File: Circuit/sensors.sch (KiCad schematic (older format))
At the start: 6 parts, among them U301 BME280, U302 ADXL345

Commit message: More BOM - passives mostly.
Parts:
- R301, R302: Digikey PN (none) -> 311-4.7KGRCT-ND; Link (none) -> http://www.digikey.com.au/product-detail/en/yageo/RC0603JR-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; Manufacturer PN (none) -> RC0603JR-074K7L; Unit Cost (none) -> 0.10
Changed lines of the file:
@@
 Connection ~ 2500 2700
-$Comp
-L R R302
-U 1 1 564CDB75
-P 2250 3050
-F 0 "R302" V 2330 3050 50  0000 C CNN
-F 1 "4.7K" V 2250 3050 50  0000 C CNN
-F 2 "Resistors_SMD:R_0603_HandSoldering" V 2350 2850 24  0000 C CNN
-F 3 "" H 2250 3050 60  0000 C CNN
-	1    2250 3050
-	1    0    0    -1
-$EndComp
 $Comp
 L R R301
@@
 F 2 "Resistors_SMD:R_0603_HandSoldering" V 2150 2750 24  0000 C CNN
 F 3 "" H 2050 2950 60  0000 C CNN
+F 4 "311-4.7KGRCT-ND" V 2050 2950 60  0001 C CNN "Digikey PN"
+F 5 "http://www.digikey.com.au/product-detail/en/yageo/RC0603JR-074K7L/311-4.7KGRCT-ND/729732" V 2050 2950 60  0001 C CNN "Link"
+F 6 "RC0603JR-074K7L" V 2050 2950 60  0001 C CNN "Manufacturer PN"
+F 7 "0.10" V 2050 2950 60  0001 C CNN "Unit Cost"
 	1    2050 2950
 	1    0    0    -1
@@
 Text Notes 1200 1350 0    60   ~ 0
 Recommend different or removal. -BP
+$Comp
+L R R302
+U 1 1 58223067
+P 2250 3050
+F 0 "R302" V 2330 3050 50  0000 C CNN
+F 1 "4.7K" V 2250 3050 50  0000 C CNN
+F 2 "Resistors_SMD:R_0603_HandSoldering" V 2350 2850 24  0000 C CNN
+F 3 "" H 2250 3050 60  0000 C CNN
+F 4 "311-4.7KGRCT-ND" V 2250 3050 60  0001 C CNN "Digikey PN"
+F 5 "http://www.digikey.com.au/product-detail/en/yageo/RC0603JR-074K7L/311-4.7KGRCT-ND/729732" V 2250 3050 60  0001 C CNN "Link"
+F 6 "RC0603JR-074K7L" V 2250 3050 60  0001 C CNN "Manufacturer PN"
+F 7 "0.10" V 2250 3050 60  0001 C CNN "Unit Cost"
+	1    2250 3050
+	1    0    0    -1
+$EndComp
 $EndSCHEMATC

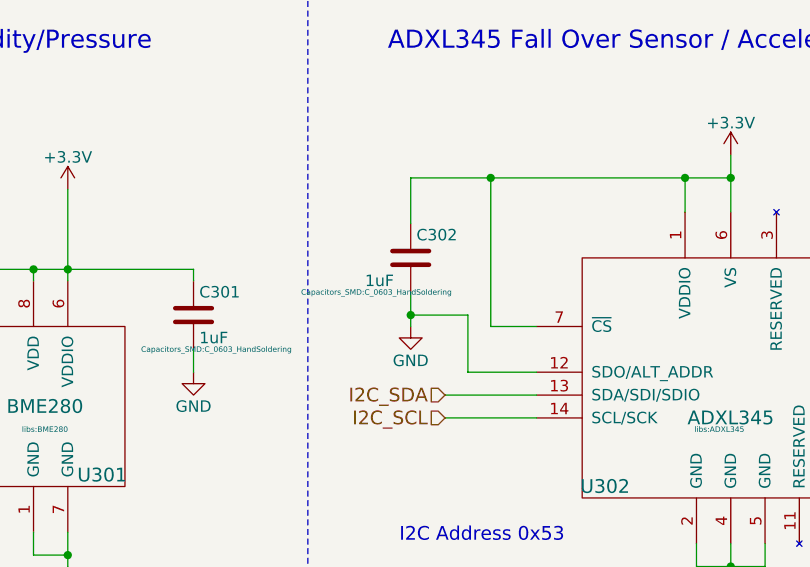
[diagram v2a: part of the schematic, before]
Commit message: Sensor ICs BOM information.
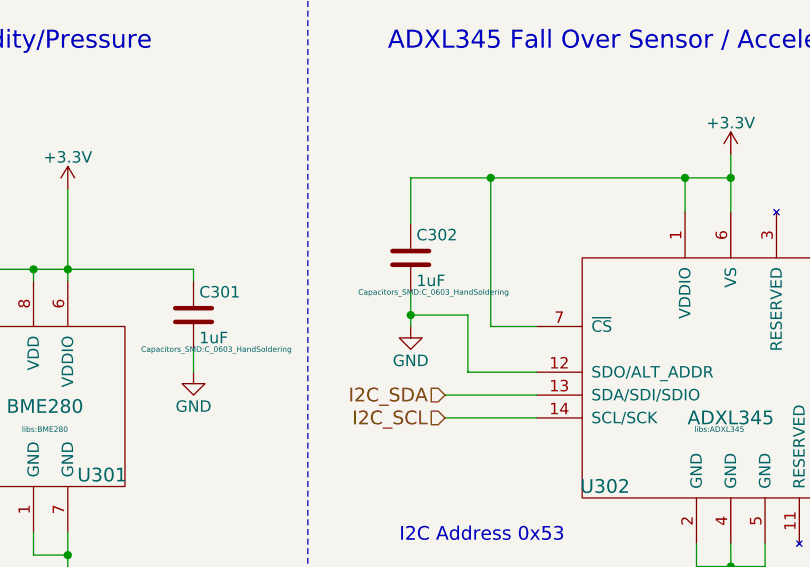
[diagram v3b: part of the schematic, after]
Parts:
- C301, C302: Digikey PN (none) -> 311-1372-1-ND; Link (none) -> http://www.digikey.com.au/product-detail/en/yageo/CC0603ZRY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; Manufacturer PN (none) -> CC0603ZRY5V7BB105; Unit Cost (none) -> 0.10
- U301: Digikey PN (none) -> 828-1063-1-ND; Link (none) -> http://www.digikey.com.au/product-detail/en/bosch-sensortec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; Manufacturer PN (none) -> BME280; Unit Cost (none) -> 11.00
- U302: Digikey PN (none) -> ADXL345BCCZ-RLCT-ND; Link (none) -> http://www.digikey.com.au/product-detail/en/analog-devices-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; Manufacturer PN (none) -> ADXL345BCCZ-RL; Unit Cost (none) -> 7.36
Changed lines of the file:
@@
 F 2 "libs:BME280" H 3150 3200 24  0000 C CNN
 F 3 "" H 3150 3300 60  0000 C CNN
+F 4 "828-1063-1-ND" H 3150 3300 60  0001 C CNN "Digikey PN"
+F 5 "http://www.digikey.com.au/product-detail/en/bosch-sensortec/BME280/828-1063-1-ND/6136314" H 3150 3300 60  0001 C CNN "Link"
+F 6 "BME280" H 3150 3300 60  0001 C CNN "Manufacturer PN"
+F 7 "11.00" H 3150 3300 60  0001 C CNN "Unit Cost"
 	1    3150 3300
 	1    0    0    -1
@@
 F 2 "libs:ADXL345" H 6100 2800 24  0000 C CNN
 F 3 "" H 6100 2800 60  0000 C CNN
+F 4 "ADXL345BCCZ-RLCT-ND" H 6150 3100 60  0001 C CNN "Digikey PN"
+F 5 "http://www.digikey.com.au/product-detail/en/analog-devices-inc/ADXL345BCCZ-RL/ADXL345BCCZ-RLCT-ND/2237841" H 6150 3100 60  0001 C CNN "Link"
+F 6 "ADXL345BCCZ-RL" H 6150 3100 60  0001 C CNN "Manufacturer PN"
+F 7 "7.36" H 6150 3100 60  0001 C CNN "Unit Cost"
 	1    6150 3100
 	1    0    0    -1
@@
 	6900 2950 7100 2950
 NoConn ~ 7100 2950
-$Comp
-L C C302
-U 1 1 564CEBB9
-P 4750 2650
-F 0 "C302" H 4775 2750 50  0000 L CNN
-F 1 "1uF" H 4550 2550 50  0000 L CNN
-F 2 "Capacitors_SMD:C_0603_HandSoldering" H 4600 2500 24  0000 C CNN
-F 3 "" H 4750 2650 60  0000 C CNN
-	1    4750 2650
-	1    0    0    -1
-$EndComp
 Wire Wire Line
 	4750 2800 4750 2950
@@
 F 2 "Capacitors_SMD:C_0603_HandSoldering" H 3900 2750 24  0000 C CNN
 F 3 "" H 3800 2900 60  0000 C CNN
+F 4 "311-1372-1-ND" H 3800 2900 60  0001 C CNN "Digikey PN"
+F 5 "http://www.digikey.com.au/product-detail/en/yageo/CC0603ZRY5V7BB105/311-1372-1-ND/2103156" H 3800 2900 60  0001 C CNN "Link"
+F 6 "CC0603ZRY5V7BB105" H 3800 2900 60  0001 C CNN "Manufacturer PN"
+F 7 "0.10" H 3800 2900 60  0001 C CNN "Unit Cost"
 	1    3800 2900
 	1    0    0    -1
@@
 	1    0    0    -1
 $EndComp
+$Comp
+L C C302
+U 1 1 58232438
+P 4750 2650
+F 0 "C302" H 4775 2750 50  0000 L CNN
+F 1 "1uF" H 4775 2550 50  0000 L CNN
+F 2 "Capacitors_SMD:C_0603_HandSoldering" H 4850 2500 24  0000 C CNN
+F 3 "" H 4750 2650 60  0000 C CNN
+F 4 "311-1372-1-ND" H 4750 2650 60  0001 C CNN "Digikey PN"
+F 5 "http://www.digikey.com.au/product-detail/en/yageo/CC0603ZRY5V7BB105/311-1372-1-ND/2103156" H 4750 2650 60  0001 C CNN "Link"
+F 6 "CC0603ZRY5V7BB105" H 4750 2650 60  0001 C CNN "Manufacturer PN"
+F 7 "0.10" H 4750 2650 60  0001 C CNN "Unit Cost"
+	1    4750 2650
+	1    0    0    -1
+$EndComp
